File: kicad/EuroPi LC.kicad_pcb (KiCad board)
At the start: 2 copper layers, 30.5 x 100 mm, 58 parts, among them J3 Conn_02x08_Odd_Even, J4 Thonkiconn, J5 Thonkiconn, J6 Thonkiconn, J7 Thonkiconn, J8 Thonkiconn, J9 Thonkiconn, P1 Potentiometer_9mm_Vertical_Li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, P2 Potentiometer_9mm_Vertical_Li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, SW1 SW_Push_LED, SW2 SW_Push_LED, U1 TL074, U2 MCP6002-xSN, U4 MOUDLE-SEEEDUINO-XIAO, U5 MCP3208

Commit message: make 4hp
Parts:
- removed D1: D, Diode_SMD:D_SOD-123
- removed J3: Conn_02x08_Odd_Even, Eurorack:Eurorack Power Header 16 Pin Unlabeled
- added C10: 100n, Capacitor_SMD:C_0402_1005Metric, B.Cu at (14.0, 21.6)
- added C11: 100n, Capacitor_SMD:C_0402_1005Metric, B.Cu at (6.35, 21.6)
- added C12: 100n, Capacitor_SMD:C_0402_1005Metric, B.Cu at (5.08, 1.91)
- added J1: Conn_02x05_Odd_Even, Eurorack:Eurorack Power Header Unlabeled, B.Cu at (10.2, 33.0)
- added U3: ~, Package_TO_SOT_SMD:SOT-89-3, B.Cu at (10.2, 23.5)
- C1, C2, C3, C4, C5, C6, C7, C8, C9, D2, D3, R1, R10, R11, R12, R13, R14, R15, R16, R17, R18, R19, R2, R20, R21, R22, R23, R24, R25, R26, R27, R3, R4, R5, R6, R7, R8, R9, U1, U2, U5: moved to B.Cu
- LED1, LED2, LED3, LED4: footprint Eurorack:LED 3mm -> allensynthesis:led-3mm
- moved C2 81.6 mm to (1.91, 21.0), turned to -90 degrees
- moved C1 79.1 mm to (18.4, 21.0), turned to 90 degrees
- moved D3 74.5 mm to (1.91, 25.4), turned to 90 degrees
- moved D2 48.6 mm to (18.4, 25.4), turned to -90 degrees
- moved C4 28.3 mm to (2.54, 74.3), turned to 90 degrees
- moved R4 27.2 mm to (1.27, 74.3), turned to 90 degrees
- moved R6 24.6 mm to (1.27, 76.8), turned to -90 degrees
- moved R2 19.3 mm to (4.45, 73.7), turned to 180 degrees
- moved C6 18.9 mm to (4.45, 72.4), turned to 0 degrees
- moved C3 17.0 mm to (17.8, 71.8), turned to -90 degrees
- moved R27 16.8 mm to (15.2, 14.6), turned to -90 degrees
- moved R12 16.6 mm to (4.45, 71.1), turned to 180 degrees
- moved R18 16.5 mm to (12.1, 87.0), turned to 180 degrees
- moved R17 16.5 mm to (12.1, 67.9), turned to 180 degrees
- moved R16 16.4 mm to (1.27, 69.2)
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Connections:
- U4 pad 14: VSYS -> +5V
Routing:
- net VSYS: track 98.5 -> 0.00 mm, vias 5 -> 0
- net Net-(R6-Pad2): track 60.1 -> 16.5 mm
- net Net-(R16-Pad2): track 59.0 -> 27.7 mm
- net OUTPUT_1: track 102.6 -> 72.6 mm, vias 5 -> 1
- net +5V: track 0.00 -> 24.9 mm, vias 0 -> 1
- net KNOB_2: track 36.4 -> 15.2 mm
- net KNOB_1: track 30.1 -> 10.9 mm
- net OUTPUT_3: track 67.3 -> 85.7 mm
- net 5V_RAIL: track 17.8 -> 0.00 mm
- net Net-(U1D-+): track 21.2 -> 6.10 mm, vias 2 -> 0
- net Net-(U1C-+): track 21.3 -> 6.13 mm, vias 2 -> 0
- net Net-(U1A-+): track 21.1 -> 6.10 mm, vias 2 -> 0
- net Net-(U1B-+): track 21.1 -> 6.13 mm, vias 2 -> 0
- net OUTPUT_4: track 65.4 -> 80.0 mm
- net +12V: track 54.4 -> 67.5 mm, vias 5 -> 2
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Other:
- board size 30.5 x 100 mm -> 20.3 x 100 mm

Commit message: kicad
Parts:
- moved R13 2.33 mm to (18.2, 76.5), turned to -90 degrees
- moved R15 1.99 mm to (18.2, 78.6)
- moved R3 1.99 mm to (18.2, 70.0)
- moved R5 1.66 mm to (18.2, 67.8)
- moved R23 0.89 mm to (17.5, 56.5)
- moved C3 0.54 mm to (18.2, 72.1)
- moved C7 0.38 mm to (18.2, 74.3)
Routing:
- net Net-(U1B--): track 20.1 -> 21.0 mm
- net Net-(U1A--): track 8.73 -> 7.82 mm
- net Net-(J9-TN): track 3.26 -> 2.38 mm
- net Earth: track 2.98 -> 3.39 mm, vias 0 -> 1
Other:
- board text added: "red stripe allen synthesis europi low cost cern ohl-s"

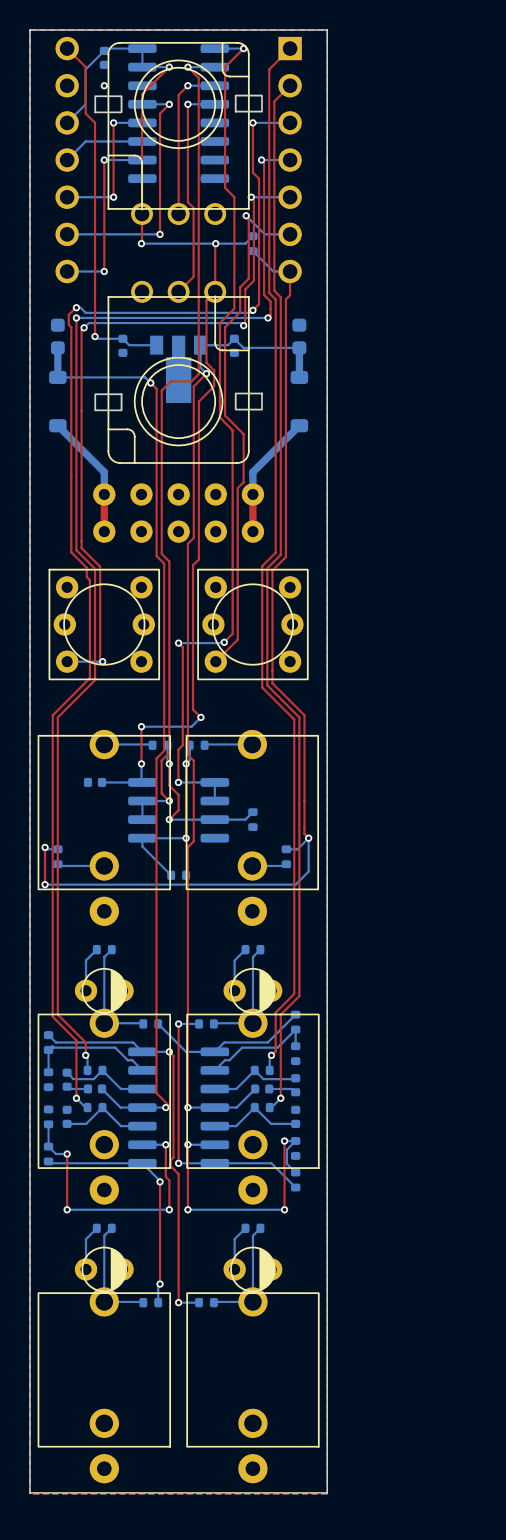
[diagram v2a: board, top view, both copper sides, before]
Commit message: input changes
use single channel ADCs for analog inputs and knob 1 which use i2c instead of SPI to free up one pin for input 1 to be used as a digital input as well
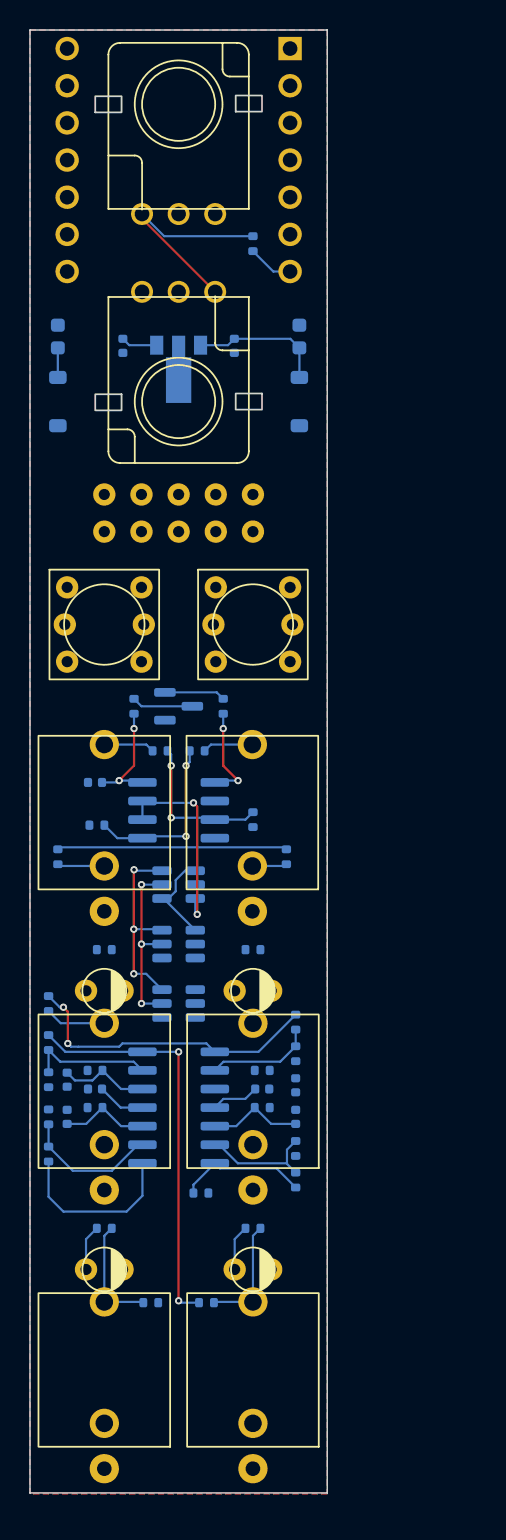
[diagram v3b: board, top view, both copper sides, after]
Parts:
- removed C12: 100n, Capacitor_SMD:C_0402_1005Metric
- added Q1: S8050, Package_TO_SOT_SMD:SOT-23, B.Cu at (10.2, 46.2)
- added R28: 100K, Resistor_SMD:R_0402_1005Metric, B.Cu at (13.2, 46.2)
- added R29: 47K, Resistor_SMD:R_0402_1005Metric, B.Cu at (7.11, 46.2)
- added U6: ADC121C027CIMK, Package_TO_SOT_SMD:TSOT-23-6, B.Cu at (10.2, 62.5)
- added U7: ADC121C027CIMK, Package_TO_SOT_SMD:TSOT-23-6, B.Cu at (10.2, 66.5)
- U4: value MOUDLE-SEEEDUINO-XIAO -> SEEEDUINO-XIAO
- U5: value MCP3208 -> ADC121C027CIMK; footprint Package_SO:SOIC-16_3.9x9.9mm_P1.27mm -> Package_TO_SOT_SMD:TSOT-23-6
- moved U5 52.7 mm to (10.2, 58.4)
- moved R17 11.6 mm to (11.7, 79.5)
- moved R7 7.12 mm to (1.27, 66.5), turned to 90 degrees
- moved R26 6.56 mm to (4.57, 54.4), turned to 180 degrees
- moved R22 0.38 mm to (8.89, 49.3)
- moved R24 0.38 mm to (11.4, 49.3)
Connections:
- U4 pad 1: OUTPUT_1 -> KNOB_2
- U4 pad 10: ADC_DOUT -> OUTPUT_2
- U4 pad 11: ADC_DIN -> OUTPUT_1
- U4 pad 2: OUTPUT_2 -> DIGITAL_INPUT
- U4 pad 3: OUTPUT_3 -> BUTTON_1
- U4 pad 4: OUTPUT_4 -> unconnected-(U4-PA11_A3_D3-Pad4)
- U4 pad 5: BUTTON_1 -> ADC_SDA
- U4 pad 6: BUTTON_2 -> ADC_SCL
- U4 pad 8: ADC_CS -> unconnected-(U4-PB09_A7_D7_RX-Pad8)
- U4 pad 9: ADC_CLK -> OUTPUT_3
- U5 pad 1: Net-(U2A--) -> +3V3
- U5 pad 2: Net-(U2B--) -> Earth
- U5 pad 3: KNOB_1 -> Net-(U2B--)
- U5 pad 4: KNOB_2 -> +3V3
- U5 pad 5: unconnected-(U5-CH4-Pad5) -> ADC_SCL
- U5 pad 6: unconnected-(U5-CH5-Pad6) -> ADC_SDA
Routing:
- net OUTPUT_3: track 85.7 -> 0.00 mm, vias 4 -> 0
- net OUTPUT_4: track 80.0 -> 0.00 mm, vias 4 -> 0
- net OUTPUT_2: track 72.7 -> 0.00 mm, vias 1 -> 0
- net OUTPUT_1: track 72.6 -> 0.00 mm, vias 1 -> 0
- net -12V: track 64.0 -> 5.31 mm, vias 2 -> 0
- net +12V: track 67.5 -> 12.5 mm, vias 2 -> 0
- net Net-(U2A--): track 61.0 -> 6.63 mm, vias 4 -> 2
- net INPUT_DETECT: track 69.4 -> 18.9 mm, vias 3 -> 0
- net BUTTON_1: track 48.8 -> 0.00 mm, vias 4 -> 0
- net +3V3: track 77.1 -> 30.1 mm, vias 6 -> 2
- net Net-(U2B--): track 57.9 -> 13.7 mm
- net BUTTON_2: track 36.1 -> 0.00 mm, vias 1 -> 0
- net +5V: track 24.9 -> 2.49 mm, vias 1 -> 0
- net ADC_CLK: track 17.3 -> 0.00 mm, vias 2 -> 0
- net KNOB_2: track 15.2 -> 0.00 mm, vias 1 -> 0
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
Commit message: reroute pcb
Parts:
- moved U7 61.5 mm to (10.2, 5.08)
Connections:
- U4 pad 4: unconnected-(U4-PA11_A3_D3-Pad4) -> BUTTON_2
- U4 pad 8: unconnected-(U4-PB09_A7_D7_RX-Pad8) -> OUTPUT_4
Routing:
- net OUTPUT_2: track 0.00 -> 83.9 mm, vias 0 -> 2
- net OUTPUT_1: track 0.00 -> 83.9 mm, vias 0 -> 2
- net ADC_SDA: track 13.4 -> 96.4 mm, vias 3 -> 7
- net ADC_SCL: track 12.3 -> 87.8 mm, vias 3 -> 6
- net +3V3: track 30.1 -> 97.9 mm, vias 2 -> 7
- net OUTPUT_3: track 0.00 -> 62.2 mm, vias 0 -> 1
- net -12V: track 5.31 -> 63.8 mm, vias 0 -> 2
- net OUTPUT_4: track 0.00 -> 56.7 mm, vias 0 -> 1
- net +12V: track 12.5 -> 68.1 mm, vias 0 -> 2
- net DIGITAL_INPUT: track 4.20 -> 58.0 mm, vias 0 -> 4
- net BUTTON_1: track 0.00 -> 51.5 mm, vias 0 -> 1
- net INPUT_DETECT: track 18.9 -> 62.1 mm, vias 0 -> 2
- net BUTTON_2: track 0.00 -> 38.8 mm, vias 0 -> 1
- net Net-(J6-T): track 0.00 -> 31.8 mm, vias 0 -> 2
- net +5V: track 2.49 -> 26.8 mm, vias 0 -> 1
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
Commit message: pcb updates
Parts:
- J1: footprint Eurorack:Eurorack Power Header Unlabeled -> allen-synthesis:power-header-10-pin-unlabelled
- J4, J5, J6, J7, J8, J9: footprint Eurorack:Thonkiconn Mono Jack -> allen-synthesis:jack-thonkiconn-mono
- LED1, LED2, LED3, LED4: footprint allensynthesis:led-3mm -> allen-synthesis:led-3mm
- P1, P2: footprint Eurorack:Potentiometer 9mm Vertical Linear Centred -> allen-synthesis:potentiometer-9mm
